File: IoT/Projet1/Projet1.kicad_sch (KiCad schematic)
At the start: 27 parts, among them J1 6120XX21621_61202021621, J2 USB4105GFA060, J3 B2B-XH-A_LF__SN_, U1 MCP73831T-2DCI_MC, U2 MCP1825S-3302E_DB, U3 ESP32-WROOM-32D, U4 TMP117MAIDRVR

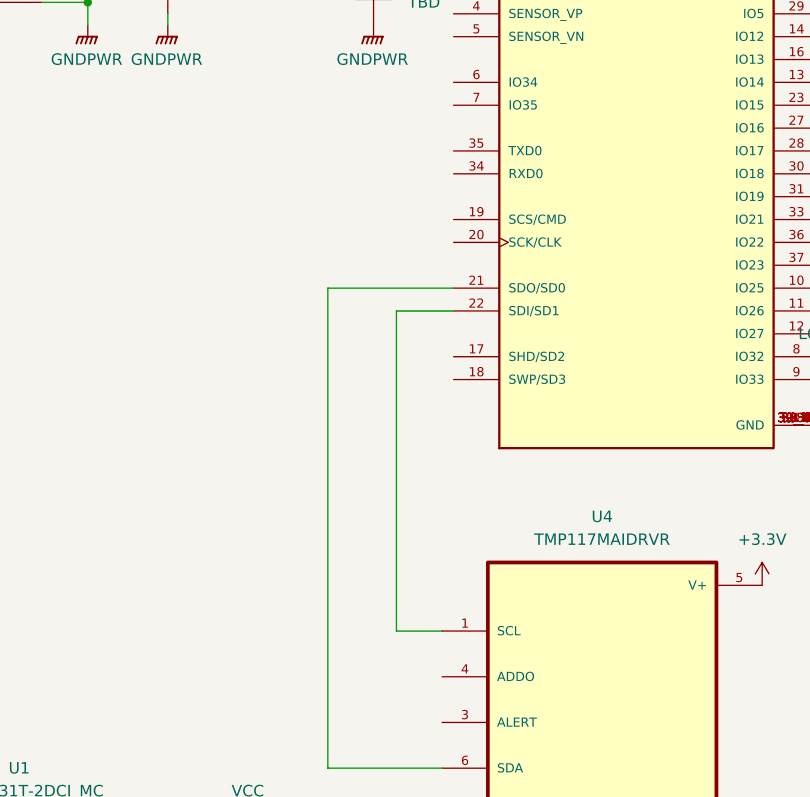
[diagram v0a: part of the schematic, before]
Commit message: Ajout R_up I2C
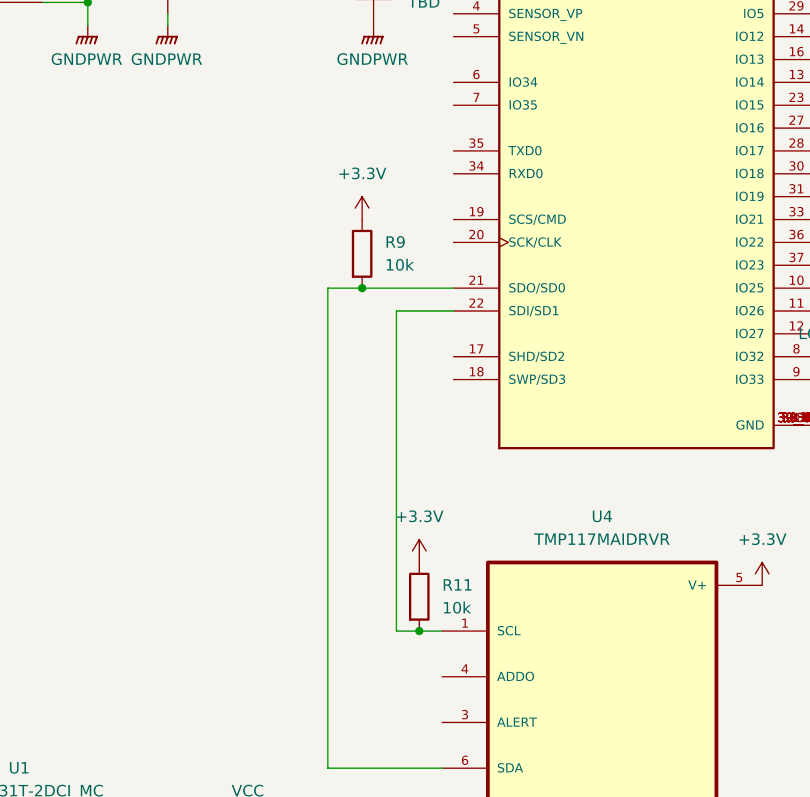
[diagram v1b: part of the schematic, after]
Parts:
- added R11, R9: 10k, Resistor_SMD:R_0805_2012Metric, symbol Device:R
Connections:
- net +3.3V: now also R11.1, R9.1
- net at U3.22 (SDI/SD1), U4.1 (SCL): now also R11.2
- net at U3.21 (SDO/SD0), U4.6 (SDA): now also R9.2
